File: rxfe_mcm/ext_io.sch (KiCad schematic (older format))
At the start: 34 parts, among them CON301 BARREL_JACK, P301 CONN_01X01, P302 CONN_01X02, Q301 DMG2305UX, T301 TRANSFO4, T302 TRANSFO4, U301 CONN_SMA, U302 CONN_SMA, U303 CONN_SMA, U304 CONN_SMA, U305 CONN_SMA, U306 CONN_SMA, U307 ADUM6400

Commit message: added some notes/errata to the transmitter schematics
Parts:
- C301: PN (none) -> P16468CT-ND
- CON301: PN (none) -> CP-002A-ND
- F301: PN (none) -> MF-USMF075-2
- L301: value FERRITE -> FBMH3225HM601NT; PN (none) -> 587-1755-1-ND
- P302: PN (none) -> 277-1273-ND
- Q301: PN (none) -> DMG2305UX-13DICT-ND
- T301, T302: PN (none) -> ETC1-1T-2TR
- U301, U302, U303, U304, U305, U306: PN (none) -> CONSMA002-L-ND
- U307: PN (none) -> ADUM6400ARWZ-ND
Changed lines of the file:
@@
 LIBS:adp7158
 LIBS:pe4312
+LIBS:rxfe_mcm-cache
 EELAYER 25 0
 EELAYER END
@@
 F 2 "Connect:BARREL_JACK" H 7900 3600 50  0001 C CNN
 F 3 "" H 7900 3600 50  0000 C CNN
+F 4 "CP-002A-ND" H 7900 3600 60  0001 C CNN "PN"
 	1    7900 3600
 	1    0    0    -1
@@
 F 2 "footprints:SMA_rightangle" H 6550 3450 60  0001 C CNN
 F 3 "" H 6550 3450 60  0000 C CNN
+F 4 "CONSMA002-L-ND" H 6550 3450 60  0001 C CNN "PN"
 	1    6550 3450
 	1    0    0    -1
@@
 F 2 "footprints:SMA_rightangle" H 6550 4500 60  0001 C CNN
 F 3 "" H 6550 4500 60  0000 C CNN
+F 4 "CONSMA002-L-ND" H 6550 4500 60  0001 C CNN "PN"
 	1    6550 4500
 	1    0    0    -1
@@
 F 2 "footprints:SMA_rightangle" H 6550 5600 60  0001 C CNN
 F 3 "" H 6550 5600 60  0000 C CNN
+F 4 "CONSMA002-L-ND" H 6550 5600 60  0001 C CNN "PN"
 	1    6550 5600
 	1    0    0    -1
@@
 F 2 "footprints:SMA_rightangle" H 6550 1400 60  0001 C CNN
 F 3 "" H 6550 1400 60  0000 C CNN
+F 4 "CONSMA002-L-ND" H 6550 1400 60  0001 C CNN "PN"
 	1    6550 1400
 	1    0    0    -1
@@
 F 2 "footprints:SMA_rightangle" H 6550 2450 60  0001 C CNN
 F 3 "" H 6550 2450 60  0000 C CNN
+F 4 "CONSMA002-L-ND" H 6550 2450 60  0001 C CNN "PN"
 	1    6550 2450
 	1    0    0    -1
@@
 F 2 "Resistors_SMD:R_1210" H 9050 3500 50  0001 C CNN
 F 3 "" H 9050 3500 50  0000 C CNN
+F 4 "MF-USMF075-2" H 9050 3500 60  0001 C CNN "PN"
 	1    9050 3500
 	1    0    0    -1
@@
 P 8650 3500
 F 0 "L301" H 8680 3540 50  0000 L CNN
-F 1 "FERRITE" H 8680 3460 50  0000 L CNN
+F 1 "FBMH3225HM601NT" H 8680 3460 50  0000 L CNN
 F 2 "Resistors_SMD:R_1210" H 8650 3500 50  0001 C CNN
 F 3 "" H 8650 3500 50  0000 C CNN
+F 4 "587-1755-1-ND" H 8650 3500 60  0001 C CNN "PN"
 	1    8650 3500
 	0    -1   -1   0
@@
 F 2 "TO_SOT_Packages_SMD:SOT-23" H 9700 3700 50  0001 C CNN
 F 3 "" H 9500 3600 50  0000 C CNN
+F 4 "DMG2305UX-13DICT-ND" H 9500 3600 60  0001 C CNN "PN"
 	1    9500 3600
 	0    -1   -1   0
@@
 F 2 "Capacitors_SMD:c_elec_6.3x5.7" H 9850 3700 50  0001 C CNN
 F 3 "" H 9850 3700 50  0000 C CNN
+F 4 "P16468CT-ND" H 9850 3700 60  0001 C CNN "PN"
 	1    9850 3700
 	1    0    0    -1
@@
 F 2 "Terminal_Blocks:TerminalBlock_Pheonix_MPT-2.54mm_2pol" H 7650 2800 50  0001 C CNN
 F 3 "" H 7650 2800 50  0000 C CNN
+F 4 "277-1273-ND" H 7650 2800 60  0001 C CNN "PN"
 	1    7650 2800
 	-1   0    0    -1
@@
 F 2 "footprints:SM-22" H 5350 6800 50  0001 C CNN
 F 3 "" H 5350 6800 50  0000 C CNN
+F 4 "ETC1-1T-2TR" H 5350 6800 60  0001 C CNN "PN"
 	1    5350 6800
 	1    0    0    -1
@@
 F 2 "footprints:SMA_rightangle" H 6550 6600 60  0001 C CNN
 F 3 "" H 6550 6600 60  0000 C CNN
+F 4 "CONSMA002-L-ND" H 6550 6600 60  0001 C CNN "PN"
 	1    6550 6600
 	1    0    0    -1
@@
 F 2 "footprints:SM-22" H 5350 5800 50  0001 C CNN
 F 3 "" H 5350 5800 50  0000 C CNN
+F 4 "ETC1-1T-2TR" H 5350 5800 60  0001 C CNN "PN"
 	1    5350 5800
 	1    0    0    -1
@@
 F 2 "Housings_SOIC:SOIC-16_7.5x10.3mm_Pitch1.27mm" H 2150 3900 60  0001 C CNN
 F 3 "" H 2150 3900 60  0001 C CNN
+F 4 "ADUM6400ARWZ-ND" H 2450 3450 60  0001 C CNN "PN"
 	1    2450 3450
 	1    0    0    -1

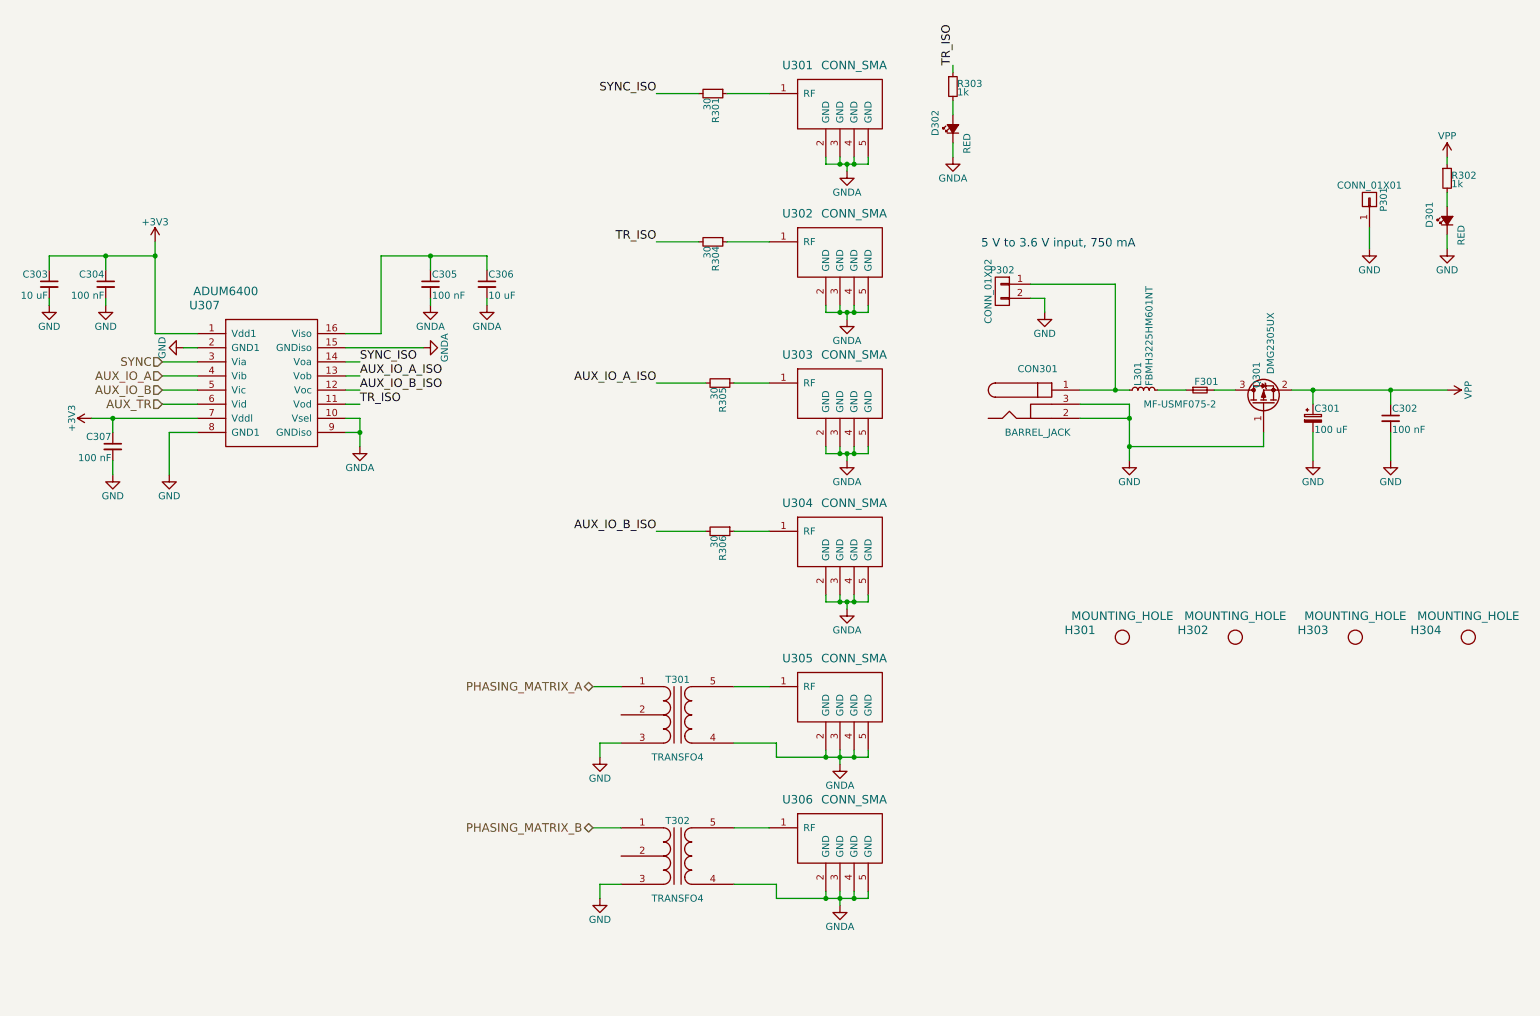
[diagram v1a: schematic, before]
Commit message: added tvs diodes to external connections on mcm_rxfe
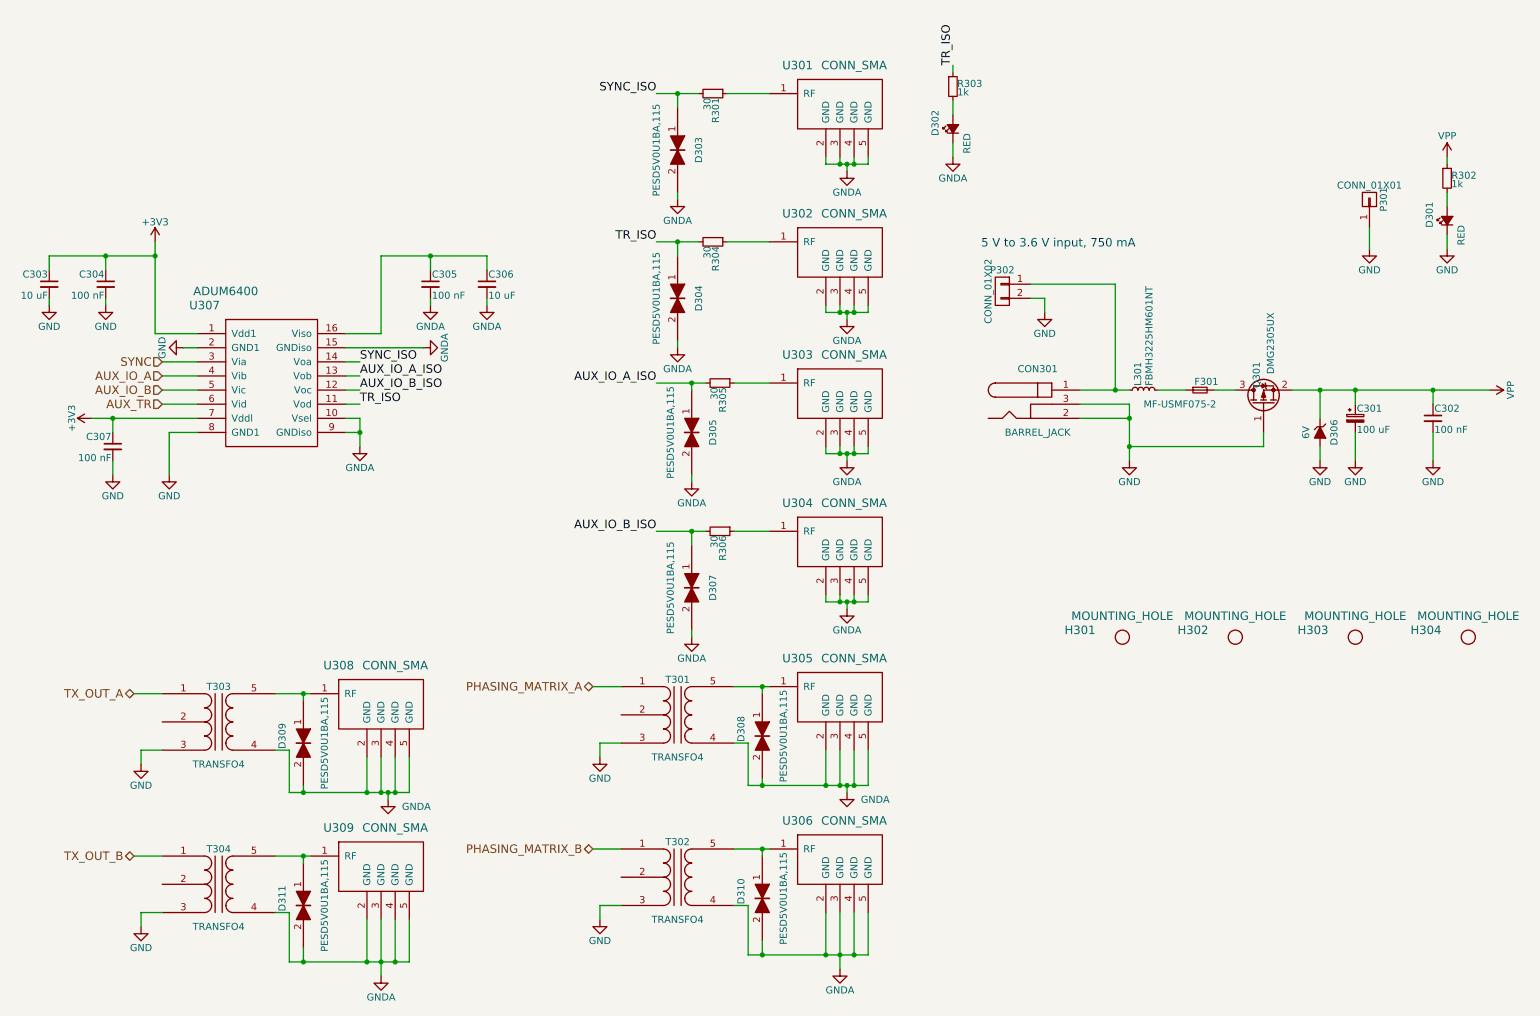
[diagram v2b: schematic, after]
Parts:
- added D303, D304, D305, D307, D308, D309, D310, D311: PESD5V0U1BA,115, Diodes_SMD:SOD-523, symbol TVS
- added D306: 6V, Diodes_SMD:SMB_Standard, symbol ZENERsmall
- added T303, T304: TRANSFO4, footprints:SM-22, symbol TRANSFO4
- added U308, U309: CONN_SMA, footprints:SMA_5-1814832-1, symbol CONN_SMA
- P301: footprint Connect:PINTST -> Pin_Headers:Pin_Header_Straight_1x01
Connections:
- net AUX_IO_A_ISO: now also D305.1
- net AUX_IO_B_ISO: now also D307.1
- net GND: now also D306.2 (A), T303.3 (PR2), T304.3 (PR2)
- net GNDA: now also D303.2, D304.2, D305.2, D307.2, D308.2, D309.2, D310.2, D311.2, T303.4 (S1), T304.4 (S1), U308.2 (GND), U308.3 (GND), U308.4 (GND), U308.5 (GND), U309.2 (GND), U309.3 (GND), U309.4 (GND), U309.5 (GND)
- net SYNC_ISO: now also D303.1
- net TR_ISO: now also D304.1
- net VPP: now also D306.1 (K)
- net at T301.5 (S2), U305.1 (RF): now also D308.1
- net at T302.5 (S2), U306.1 (RF): now also D310.1
- new net: D309.1, T303.5 (S2), U308.1 (RF)
- new net: D311.1, T304.5 (S2), U309.1 (RF)
- new net TX_OUT_A: T303.1 (PR1)
- new net TX_OUT_B: T304.1 (PR1)
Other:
- moved on the sheet: C301, C302, T302, U306

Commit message: add input protection to mcm usrp front end, modified to also work at kodiak
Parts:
- removed H301, H302, H303, H304: MOUNTING_HOLE, Mounting_Holes:MountingHole_3.2mm_M3, symbol MOUNTING_HOLE
- added D312, D313: D, Diodes_SMD:SMB_Standard, symbol D
- added D314, D315: PESD5V0U1BA,115, Diodes_SMD:SOD-523, symbol TVS
- added H305, H306, H307, H308: MOUNTING_HOLE, Mounting_Holes:MountingHole_6.5mm, symbol MOUNTING_HOLE
- added P303, P304: CONN_02X01, Pin_Headers:Pin_Header_Straight_1x02, symbol CONN_02X01
- added T305, T306: TRANSFO4, footprints:SM-22, symbol TRANSFO4
- added U310, U311: CONN_SMA, footprints:SMA_5-1814832-1, symbol CONN_SMA
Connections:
- net GND: now also T305.3 (PR2), T306.3 (PR2)
- net GNDA: now also D314.2, D315.2, P303.2 (P2), P304.2 (P2), T305.4 (S1), T306.4 (S1), U310.2 (GND), U310.3 (GND), U310.4 (GND), U310.5 (GND), U311.2 (GND), U311.3 (GND), U311.4 (GND), U311.5 (GND)
- net at CON301.1, L301.1: now also D313.1 (K); no longer P302.1 (P1)
- net at R304.1, U302.1 (RF): now also P303.1 (P1), P304.1 (P1)
- new net: D312.2 (A), P302.1 (P1)
- new net: D312.1 (K), D313.2 (A)
- new net: D314.1, T305.5 (S2), U310.1 (RF)
- new net: D315.1, T306.5 (S2), U311.1 (RF)
- new net CPL_A: T305.1 (PR1)
- new net CPL_B: T306.1 (PR1)
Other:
- note added: "6 V from USRP daughterboard"
- note added: "AUX output A,\ncould be used to gate a target"
- note added: "AUX output B"
- note added: "CPL:\nMCM - DNP\nKOD - to coupler board"
- note added: "PHASING_MATRIX:\nMAX INPUT, NO DAMAGE: 4Vpp\nMCM - multiplexed TX/RX, output to McMurdo transmitter\nKOD - RX input, to HPTR RX"
- note added: "SMA SYNC\nfor debugging"
- note added: "SMA TR\nfor MCM, to TR distro box"
- note added: "TRANSMITTER GROUND\n`GNDA`"
- note added: "TRANSMITTER-SIDE IO"
- note added: "TX_OUT:\nMCM - DNP\nKOD - to driver amplifier input"
- note added: "USRP GROUND\n`GND`"
- note added: "headers for TR signal\nfor kodiak control board"
- note added: "large mounting holes, for kodiak transmitter shelf\nspace holes along the longer axis (length) a multiple of 3/4 inches apart\nspace holes along the shorter axis (width) a multiple of 5/8 inches apart"
- moved on the sheet: C301, C302, C303, C304, C305, C306, C307, CON301, D301, D302, D303, D304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

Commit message: a bit of work on layout..
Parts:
- added P305: CONN_02X01, Pin_Headers:Pin_Header_Straight_1x02, symbol CONN_02X01
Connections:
- net GNDA: now also P305.2 (P2)
- net at R305.1, U303.1 (RF): now also P305.1 (P1)

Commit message: removed tx path amp, erc fixes
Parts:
- removed P303, P304, P305: CONN_02X01, Pin_Headers:Pin_Header_Straight_1x02, symbol CONN_02X01
- added C308, C309: 100 nF, Capacitors_SMD:C_0603, symbol C_Small
- added P303, P304, P305, P306: CONN_01X03, footprints:header_th_0705430002, symbol CONN_01X03
- added R307, R309: 4k7, Resistors_SMD:R_0603, symbol R_Small
- added R308, R310: 1k, Resistors_SMD:R_0603, symbol R_Small
- added U312, U313: ISL3295EFHZ-T, TO_SOT_Packages_SMD:SOT-23-6, symbol ISL3295EFHZ-T
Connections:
- net GNDA: now also C308.2, C309.2, P303.2 (P2), P304.2 (P2), P305.3 (P3), P306.3 (P3), U312.5 (GND), U313.5 (GND)
- net TR_ISO: now also U312.1 (DI), U313.1 (DI)
- net at R306.1, U304.1 (RF): now also P305.2 (P2), P306.2 (P2)
- net +3.3VP: now reaches C305.1, C306.1, U307.16 (Viso)
- net +3.3VP: now also C308.1, C309.1, R308.2, R310.2, U312.2 (Vcc), U313.2 (Vcc)
- new net: P303.1 (P1), R307.2, U312.6 (Y)
- new net: P303.3 (P3), R307.1, U312.4 (~Y)
- new net: R308.1, U312.3 (DE)
- new net: P304.1 (P1), R309.2, U313.6 (Y)
- new net: P304.3 (P3), R309.1, U313.4 (~Y)
- new net: R310.1, U313.3 (DE)
- no-connect marks 0 -> 8
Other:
- note added: "AUX output B\nadd disable jumper"
- note added: "headers for T/R output to control boards"
- note removed: "AUX output B"
- moved on the sheet: D303, D304, D305, D307, R301, R304, R305, R306, U301, U302, U303, U304

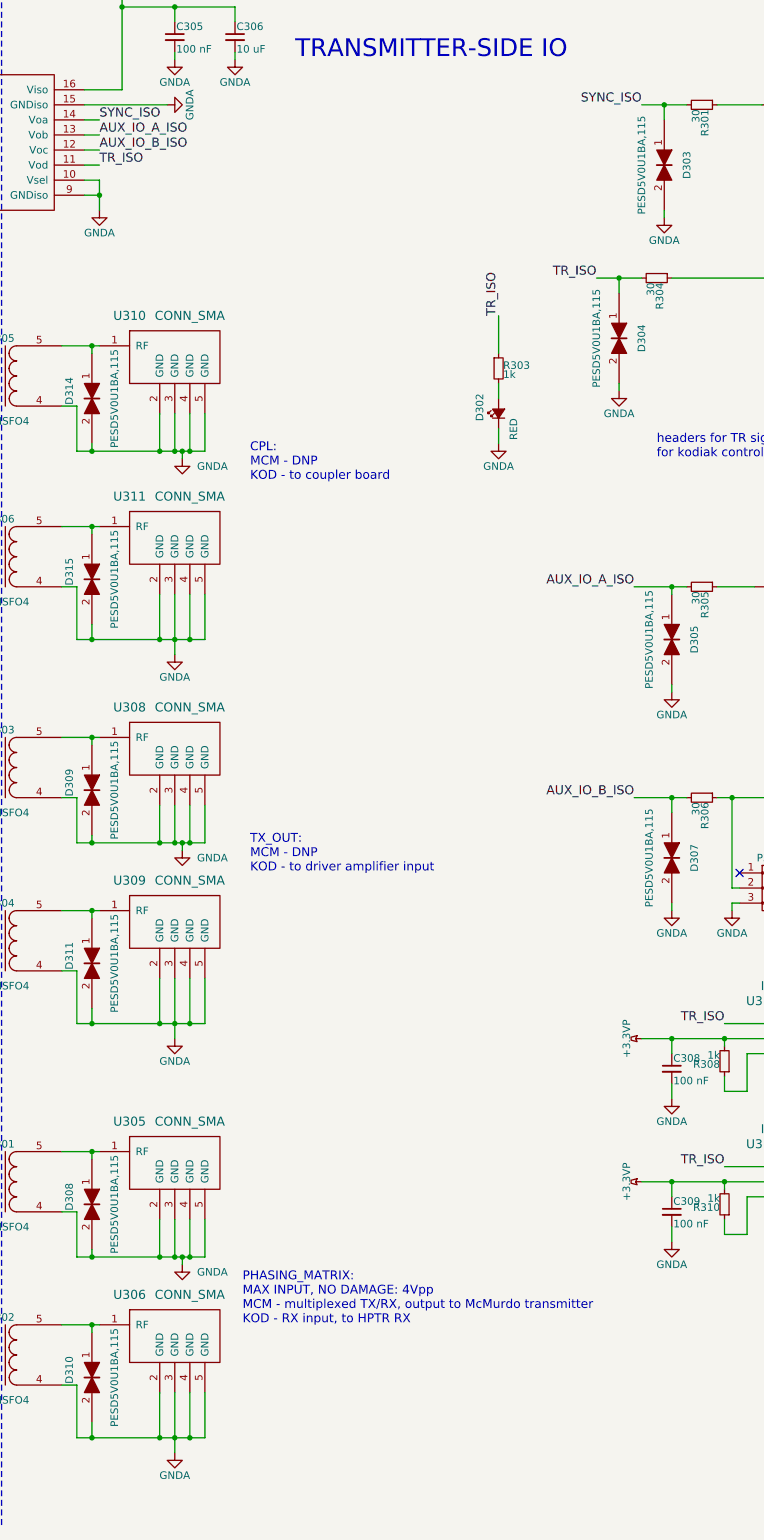
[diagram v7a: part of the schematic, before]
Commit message: moved limiter diode to fix short
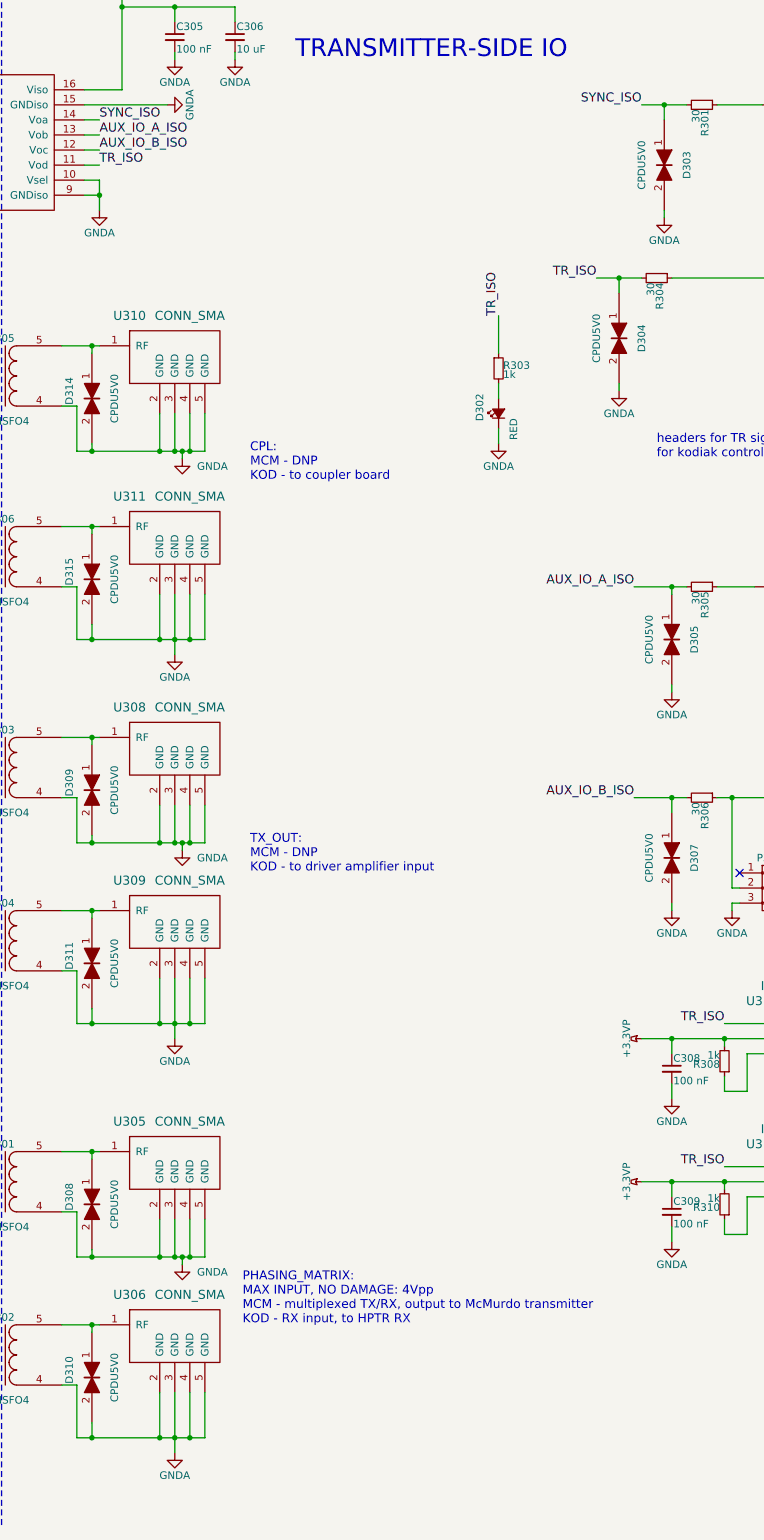
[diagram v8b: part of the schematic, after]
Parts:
- D303, D304, D305, D307, D308, D309, D310, D311, D314, D315: value PESD5V0U1BA,115 -> CPDU5V0
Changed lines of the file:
@@
 P 12950 5100
 F 0 "D305" H 12950 5250 50  0000 C CNN
-F 1 "PESD5V0U1BA,115" H 12950 4950 50  0000 C CNN
+F 1 "CPDU5V0" H 12950 4950 50  0000 C CNN
 F 2 "Diodes_SMD:SOD-523" H 12950 5100 50  0001 C CNN
 F 3 "" H 12950 5100 50  0000 C CNN
@@
 P 12950 6550
 F 0 "D307" H 12950 6700 50  0000 C CNN
-F 1 "PESD5V0U1BA,115" H 12950 6400 50  0000 C CNN
+F 1 "CPDU5V0" H 12950 6400 50  0000 C CNN
 F 2 "Diodes_SMD:SOD-523" H 12950 6550 50  0001 C CNN
 F 3 "" H 12950 6550 50  0000 C CNN
@@
 P 12600 3100
 F 0 "D304" H 12600 3250 50  0000 C CNN
-F 1 "PESD5V0U1BA,115" H 12600 2950 50  0000 C CNN
+F 1 "CPDU5V0" H 12600 2950 50  0000 C CNN
 F 2 "Diodes_SMD:SOD-523" H 12600 3100 50  0001 C CNN
 F 3 "" H 12600 3100 50  0000 C CNN
@@
 P 12900 1950
 F 0 "D303" H 12900 2100 50  0000 C CNN
-F 1 "PESD5V0U1BA,115" H 12900 1800 50  0000 C CNN
+F 1 "CPDU5V0" H 12900 1800 50  0000 C CNN
 F 2 "Diodes_SMD:SOD-523" H 12900 1950 50  0001 C CNN
 F 3 "" H 12900 1950 50  0000 C CNN
@@
 P 9100 10000
 F 0 "D310" H 9050 9850 50  0000 C CNN
-F 1 "PESD5V0U1BA,115" H 9100 10150 50  0000 C CNN
+F 1 "CPDU5V0" H 9100 10150 50  0000 C CNN
 F 2 "Diodes_SMD:SOD-523" H 9100 10000 50  0001 C CNN
 F 3 "" H 9100 10000 50  0000 C CNN
@@
 P 9100 8850
 F 0 "D308" H 9050 8700 50  0000 C CNN
-F 1 "PESD5V0U1BA,115" H 9100 9000 50  0000 C CNN
+F 1 "CPDU5V0" H 9100 9000 50  0000 C CNN
 F 2 "Diodes_SMD:SOD-523" H 9100 8850 50  0001 C CNN
 F 3 "" H 9100 8850 50  0000 C CNN
@@
 P 9100 7250
 F 0 "D311" H 9050 7100 50  0000 C CNN
-F 1 "PESD5V0U1BA,115" H 9100 7400 50  0000 C CNN
+F 1 "CPDU5V0" H 9100 7400 50  0000 C CNN
 F 2 "Diodes_SMD:SOD-523" H 9100 7250 50  0001 C CNN
 F 3 "" H 9100 7250 50  0000 C CNN
@@
 P 9100 6100
 F 0 "D309" H 9050 5950 50  0000 C CNN
-F 1 "PESD5V0U1BA,115" H 9100 6250 50  0000 C CNN
+F 1 "CPDU5V0" H 9100 6250 50  0000 C CNN
 F 2 "Diodes_SMD:SOD-523" H 9100 6100 50  0001 C CNN
 F 3 "" H 9100 6100 50  0000 C CNN
@@
 P 9100 4700
 F 0 "D315" H 9050 4550 50  0000 C CNN
-F 1 "PESD5V0U1BA,115" H 9100 4850 50  0000 C CNN
+F 1 "CPDU5V0" H 9100 4850 50  0000 C CNN
 F 2 "Diodes_SMD:SOD-523" H 9100 4700 50  0001 C CNN
 F 3 "" H 9100 4700 50  0000 C CNN
@@
 P 9100 3500
 F 0 "D314" H 9050 3350 50  0000 C CNN
-F 1 "PESD5V0U1BA,115" H 9100 3650 50  0000 C CNN
+F 1 "CPDU5V0" H 9100 3650 50  0000 C CNN
 F 2 "Diodes_SMD:SOD-523" H 9100 3500 50  0001 C CNN
 F 3 "" H 9100 3500 50  0000 C CNN
